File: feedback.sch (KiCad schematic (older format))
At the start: 1 part

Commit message: V0 schematic complete (?)
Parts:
- removed J?: CONN_01X07, symbol CONN_01X07
- added C? (x4): 100 nF C0G 1%, symbol C_Small
- added C? (x11): DNP, symbol C_Small
- added C? (x3): 1uF, symbol C_Small
- added D? (x3): RS1MSWFQ, symbol D_Small
- added D?: BZT52B7V5, symbol ZENERsmall
- added J? (x4): CONN_01X03, symbol CONN_01X03
- added P?: CONN_01X02, symbol CONN_01X02
- added P?: CONN_02X05, symbol CONN_02X05
- added R? (x8): 150K 1% 250V 0.5W, symbol R_Small
- added R? (x4): 1.8K 1%, symbol R_Small
- added R? (x2): DNP, symbol R_Small
- added R? (x7): 1.8K, symbol R_Small
- added R? (x7): 3.3K, symbol R_Small
- added R?: 2.2K, symbol R_Small
- added R? (x3): 1k, symbol R_Small
- added R?: 0R, symbol R_Small
- added R?: 750, symbol R_Small
- added U? (x3): MAX4195, symbol MAX4195
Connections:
- net labels added: +15V, +5VA, +7.5V, IFB_A, IFB_B, IFB_BUS, IFB_C, MOTOR_TEMP, PWR_TEMP_IN, VFB_A, VFB_B, VFB_BUS, VFB_C, Vds_A, Vds_B, Vds_C, VsL_A, VsL_B, VsL_C
- wire segments 6 -> 177
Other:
- note added: "Current feedback: Hall-effect sensors e.g. AMP300"
- note added: "El crappo shunt regulator"
- note added: "KTY81/210:\n1.5k at -10 C\n4.3k at +150 C"
- note added: "Low-side Vds(on) measurement as alternative form of current feedback"
- note added: "Motor temperature"
- note added: "Power stage temperature\n(will need some hacks)"
- note added: "Todo: Vphase peak detection"
- note added: "Voltage feedback"

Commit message: Annotate, fix schematic DRC, footprint for DIMM100
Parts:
- gave numbers to parts that had none: 65

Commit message: Footprints assigned, netlist generated - ready for layout
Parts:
- C10, C11, C15, C16: footprint (none) -> Capacitors_SMD:C_1206
- C12, C13, C14, C17, C18, C19, C20, C21, C22, C23, C24, C7, C8, C9: footprint (none) -> Capacitors_SMD:C_0805
- D2, D3, D4: footprint (none) -> Diodes_SMD:SOD-123
- D5: value BZT52B7V5 -> BZT52B6V8; footprint (none) -> Diodes_SMD:SOD-123
- J10: renamed from J4; footprint (none) -> sictroller:Molex-SL-3POS-RA
- J11: renamed from J5; footprint (none) -> sictroller:Molex-SL-3POS-RA
- J6: renamed from P4; footprint (none) -> Connectors_Molex:Connector_Microfit3_Header_02x05_Angled_43045-100x
- J7: renamed from P5; footprint (none) -> sictroller:Molex-SL-2POS-RA
- J8: renamed from J2; footprint (none) -> sictroller:Molex-SL-3POS-RA
- J9: renamed from J3; footprint (none) -> sictroller:Molex-SL-3POS-RA
- R10, R11, R12, R13, R14, R15, R16, R17, R18, R19, R20, R21, R22, R23, R24, R25, R26, R27, R28, R29, R3, R30, R31, R32, R33, R34, R35, R36, R4, R5, R6, R7, R8, R9: footprint (none) -> Resistors_SMD:R_0805
- U3, U4, U5: footprint (none) -> SMD_Packages:SOIC-8-N
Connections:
- net +7.5V renamed +7V
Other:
- note added: "KTY81/210 temp sensor\n -10 C: 1.5k => 2.97 V\n+150 C: 4.3k => 1.69 V"
- note removed: "KTY81/210:\n1.5k at -10 C\n4.3k at +150 C"

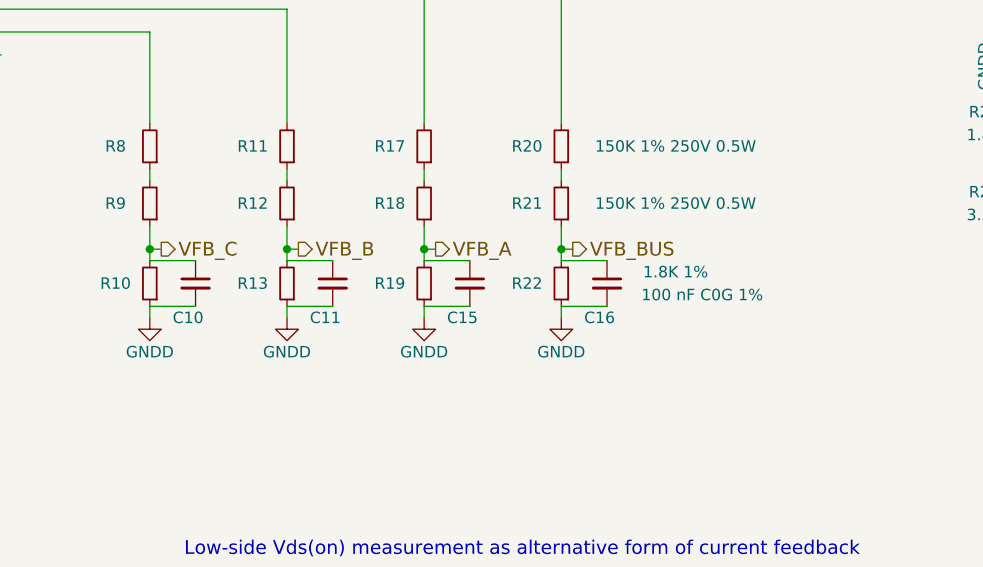
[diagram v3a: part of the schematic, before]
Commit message: More aux pins, SKUs for some components
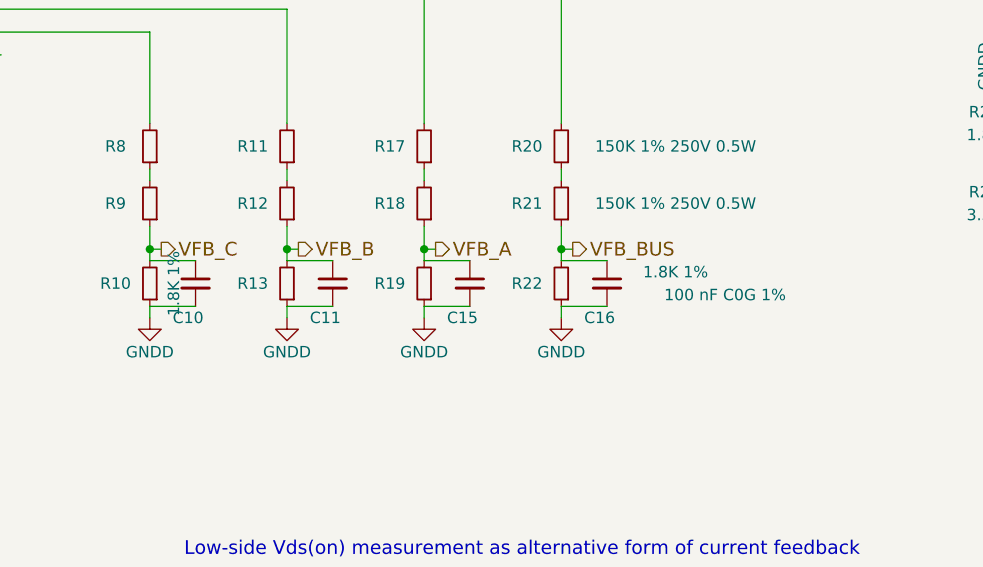
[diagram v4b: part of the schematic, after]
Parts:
- C10: footprint Capacitors_SMD:C_1206 -> Capacitors_SMD:C_1210; SKU (none) -> PCF1189CT-ND
- C11, C15, C16: footprint Capacitors_SMD:C_1206 -> Capacitors_SMD:C_1210
- C12, C13, C14, C17, C18, C19, C20, C21, C22, C23, C24, C7, C8, C9: footprint Capacitors_SMD:C_0805 -> Capacitors_SMD:C_0603
- D2: SKU (none) -> 745C101103JPCT-ND
- R10, R13, R14, R15, R16, R19, R22, R23, R24, R25, R26, R27, R28, R29, R3, R30, R31, R32, R33, R34, R35, R36, R4, R5, R6, R7: footprint Resistors_SMD:R_0805 -> Resistors_SMD:R_0603
- R8: SKU (none) -> 667-ERJ-P06F1503V; Supplier (none) -> Mouser

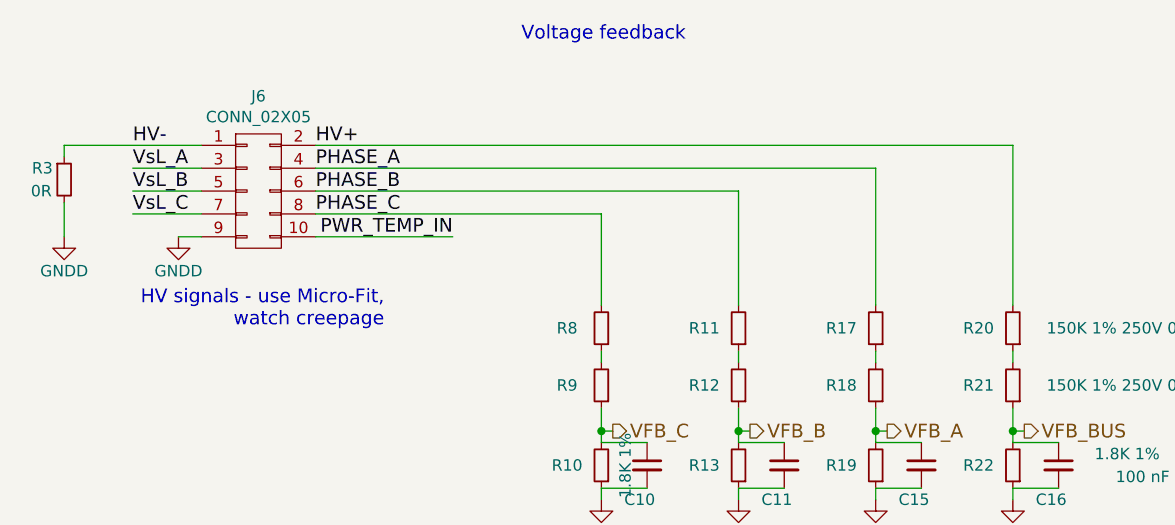
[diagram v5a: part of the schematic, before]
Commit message: Change J6 (microfit) pinning for better routing of HV
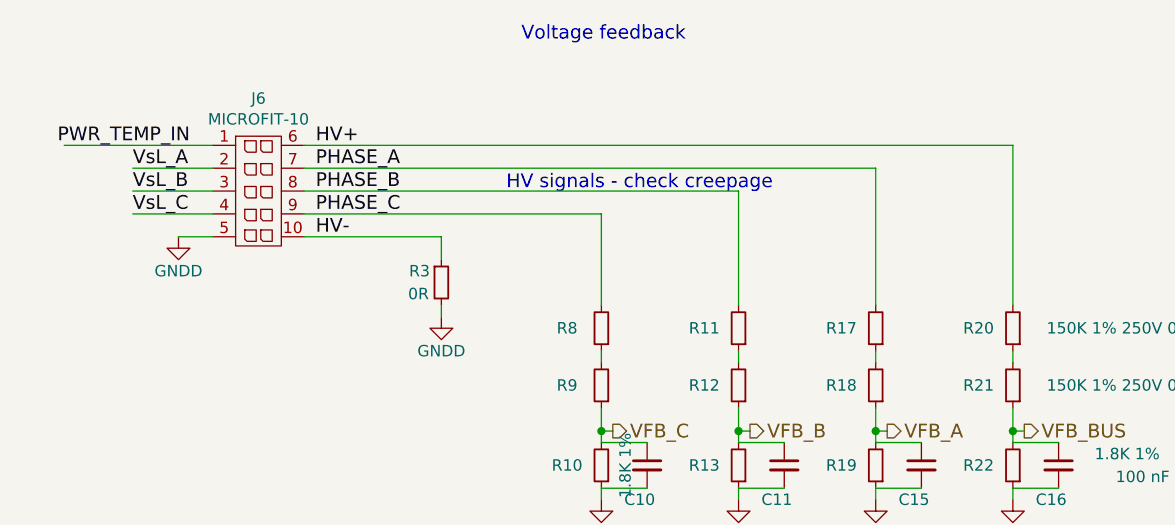
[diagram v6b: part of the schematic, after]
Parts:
- removed J6: CONN_02X05, Connectors_Molex:Connector_Microfit3_Header_02x05_Angled_43045-100x, symbol CONN_02X05
- added J6: MICROFIT-10, Connectors_Molex:Connector_Microfit3_Header_02x05_Angled_43045-100x, symbol MICROFIT-10
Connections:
- net GNDD: now also J6.5 (P5)
- net HV+: now also J6.6 (P6)
- net HV-: now also J6.10 (P10)
- net PHASE_A: now also J6.7 (P7)
- net PHASE_B: now also J6.8 (P8)
- net PHASE_C: now also J6.9 (P9)
- net PWR_TEMP_IN: now also J6.1 (P1)
- net VsL_A: now also J6.2 (P2)
- net VsL_B: now also J6.3 (P3)
- net VsL_C: now also J6.4 (P4)
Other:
- note added: "HV signals - check creepage"
- note removed: "HV signals - use Micro-Fit, \nwatch creepage"
- moved on the sheet: R3

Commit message: Routing progress
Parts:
- added C28, C29, C30, C31, C32, C33, C34, C35, C36: 470pF, Capacitors_SMD:C_0603, symbol C_Small
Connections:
- net GNDD: now also C28.2, C29.2, C30.2, C31.2, C32.2, C33.2, C34.2, C35.2, C36.2
- net MOTOR_TEMP: now also C32.1
- net VFB_A: now also C30.1
- net VFB_B: now also C29.1
- net VFB_BUS: now also C31.1
- net VFB_C: now also C28.1
- net at J8.3 (P3), R26.2: now also C33.1
- net at J9.3 (P3), R28.2: now also C34.1
- net at J10.3 (P3), R32.2: now also C35.1
- net at J11.3 (P3), R35.2: now also C36.1
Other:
- note added: "Place C28/29/30/31\nnear signal entrance"
- moved on the sheet: C10, C11, C15, C16, J6, R10, R11, R12, R13, R17, R18, R19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

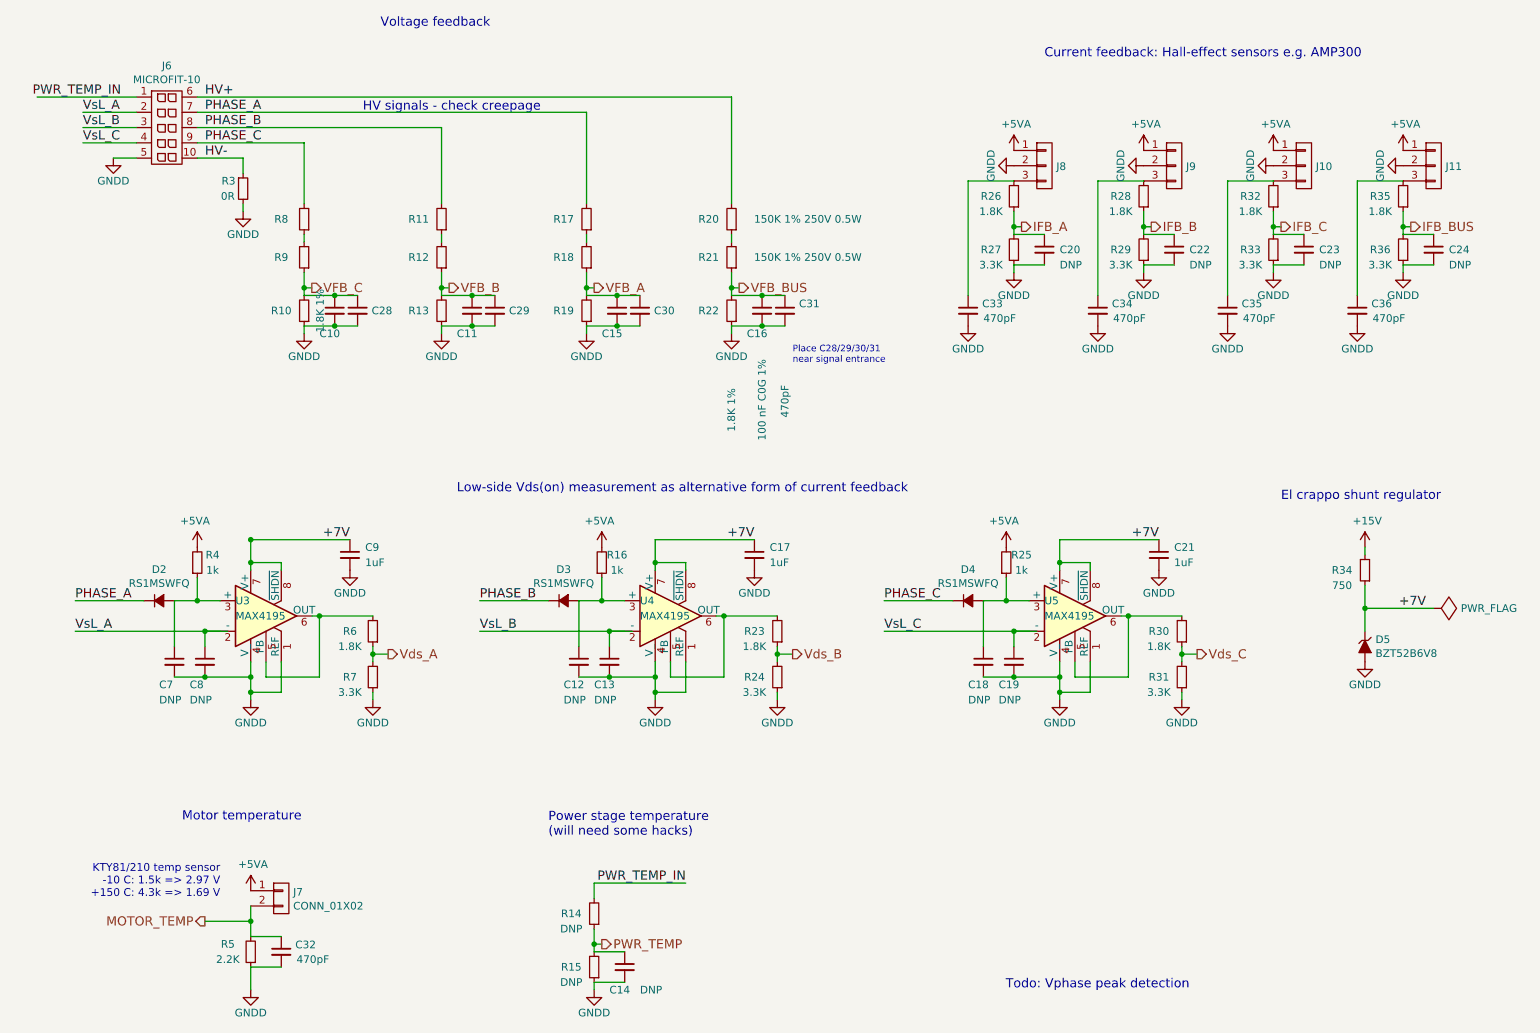
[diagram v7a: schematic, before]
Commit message: Delete Vds FB
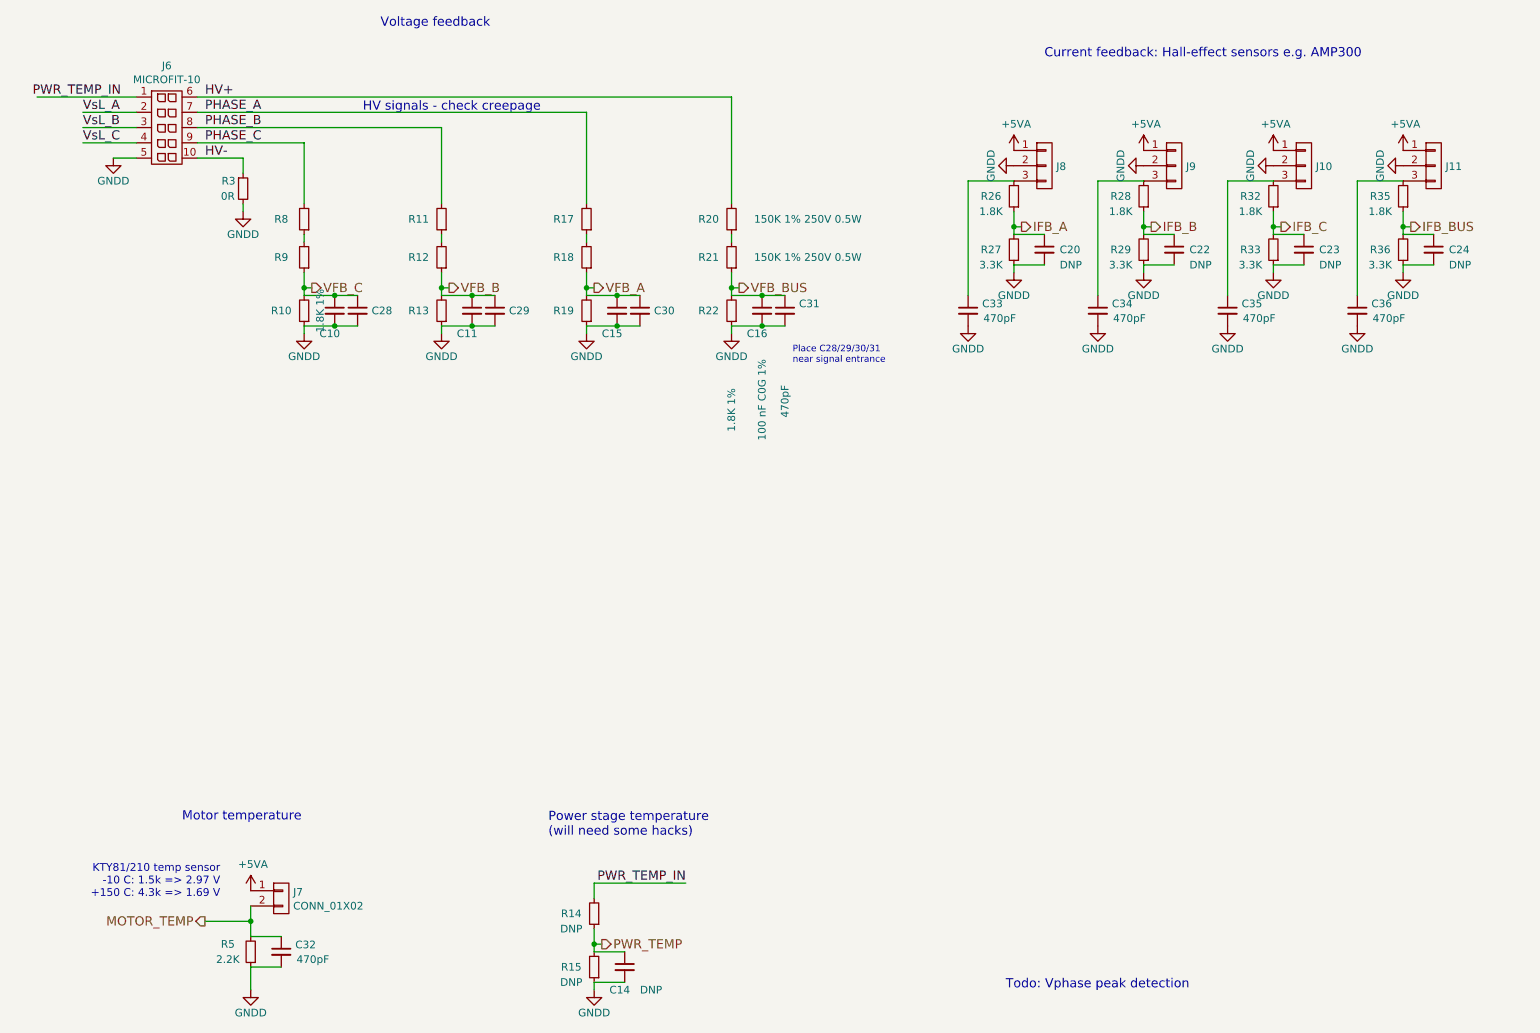
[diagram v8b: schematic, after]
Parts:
- removed C12, C13, C18, C19, C7, C8: DNP, Capacitors_SMD:C_0603, symbol C_Small
- removed C17, C21, C9: 1uF, Capacitors_SMD:C_0603, symbol C_Small
- removed D2, D3, D4: RS1MSWFQ, Diodes_SMD:SOD-123, symbol D_Small
- removed D5: BZT52B6V8, Diodes_SMD:SOD-123, symbol ZENERsmall
- removed R16, R25, R4: 1k, Resistors_SMD:R_0603, symbol R_Small
- removed R23, R30, R6: 1.8K, Resistors_SMD:R_0603, symbol R_Small
- removed R24, R31, R7: 3.3K, Resistors_SMD:R_0603, symbol R_Small
- removed R34: 750, Resistors_SMD:R_0603, symbol R_Small
- removed U3, U4, U5: MAX4195, SMD_Packages:SOIC-8-N, symbol MAX4195
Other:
- note removed: "El crappo shunt regulator"
- note removed: "Low-side Vds(on) measurement as alternative form of current feedback"
